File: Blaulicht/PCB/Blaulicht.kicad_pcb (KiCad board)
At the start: 2 copper layers, 35 x 31 mm, 11 parts, among them U1 ATtiny45V-10PU

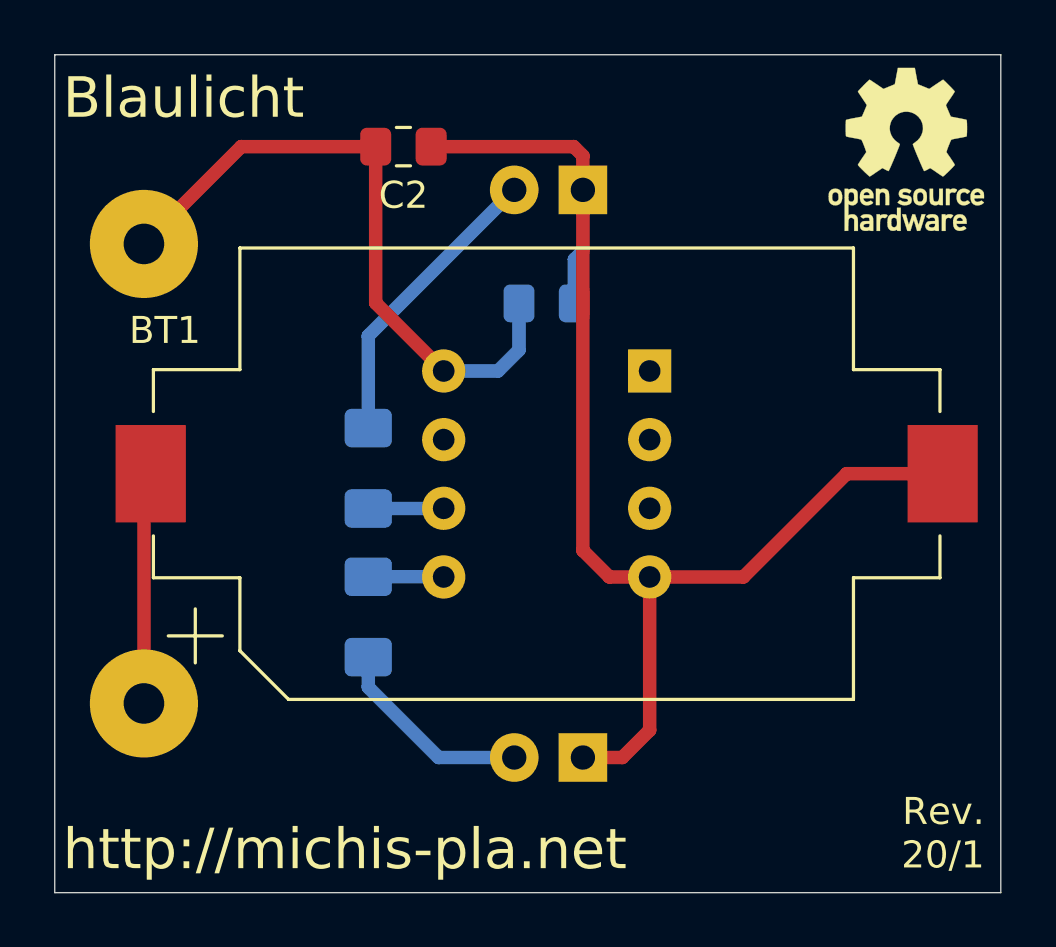
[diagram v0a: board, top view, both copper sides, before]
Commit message: Add GND fill.
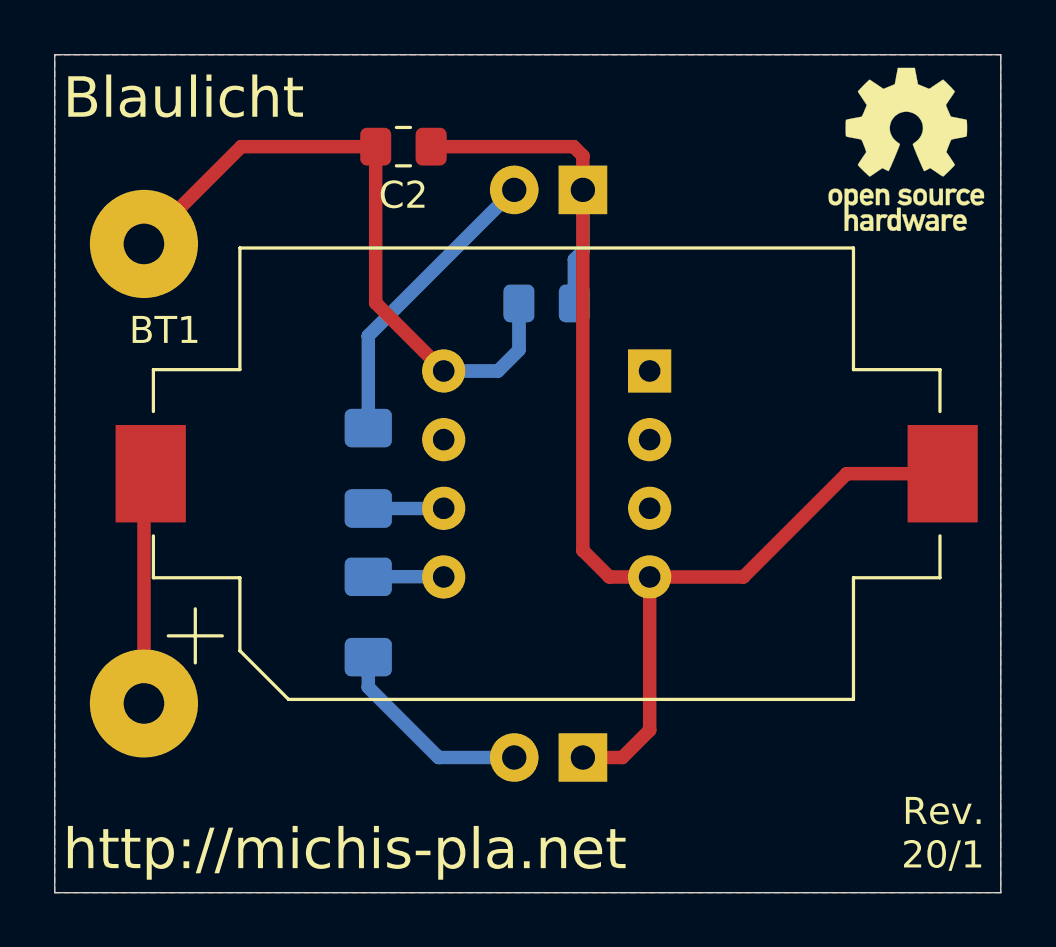
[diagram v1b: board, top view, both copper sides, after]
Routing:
- added copper zone on B.Cu, net GND
- added copper zone on F.Cu, net GND
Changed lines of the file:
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@@
   )
   (setup
-    (last_trace_width 0.5)
+    (last_trace_width 0.25)
     (user_trace_width 0.5)
     (trace_clearance 0.2)
@@
   (segment (start 117.175 95.425) (end 117.175 93.7) (width 0.5) (layer B.Cu) (net 2))
   (segment (start 116.4 96.2) (end 117.175 95.425) (width 0.5) (layer B.Cu) (net 2))
+  (segment (start 103.3 100.25) (end 103.55 100) (width 0.5) (layer F.Cu) (net 7))
+  (segment (start 103.3 108.5) (end 103.3 100.25) (width 0.5) (layer F.Cu) (net 7))
   (segment (start 111.6 94.9) (end 117 89.5) (width 0.5) (layer B.Cu) (net 8))
   (segment (start 111.6 98.3125) (end 111.6 94.9) (width 0.5) (layer B.Cu) (net 8))
@@
   (segment (start 114.3825 103.8125) (end 114.39 103.82) (width 0.5) (layer B.Cu) (net 11))
   (segment (start 111.6 103.8125) (end 114.3825 103.8125) (width 0.5) (layer B.Cu) (net 11))
-  (segment (start 103.3 100.25) (end 103.55 100) (width 0.5) (layer F.Cu) (net 7))
-  (segment (start 103.3 108.5) (end 103.3 100.25) (width 0.5) (layer F.Cu) (net 7))
+  (zone (net 1) (net_name GND) (layer F.Cu) (hatch edge 0.508)
+    (connect_pads (clearance 0.508))
+    (min_thickness 0.254)
+    (fill yes (arc_segments 32) (thermal_gap 0.508) (thermal_bridge_width 0.508))
+    (polygon
+      (pts
+        (xy 135 115.5) (xy 100 115.5) (xy 100 84.5) (xy 135 84.5)
+      )
+    )
+  )
+  (zone (net 1) (net_name GND) (layer B.Cu) (hatch edge 0.508)
+    (connect_pads (clearance 0.508))
+    (min_thickness 0.254)
+    (fill yes (arc_segments 32) (thermal_gap 0.508) (thermal_bridge_width 0.508))
+    (polygon
+      (pts
+        (xy 135 115.5) (xy 100 115.5) (xy 100 84.5) (xy 135 84.5)
+      )
+    )
+  )
 )
